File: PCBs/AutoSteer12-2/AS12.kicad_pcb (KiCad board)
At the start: 2 copper layers, 159 x 152 mm, 88 parts, among them IC1 PCA9306DCUR, IC2 XL2596, IC3 AZ1117, J1 ADS1115, J10 Conn_01x08_Female, J11 Teensy_Ethernet, J12 HR911105A, J13 Conn_01x15_Female, J14 Conn_01x08_Female, J15 Motor 2, J16 Motor 1, J17 SF_F9P_left, J18 ArduSimple_tl, J19 ArduSimple_bl, J2 WemosD1_left, J20 SF_F9P_right, J21 ArduSimple_tr, J22 ArduSimple_br, J23 Grove, J24 WemosD1_right, J25 RS485, J3 DT13-12PA, J4 CMPS14, J5 BNO080_left, J6 BNO080_right, J7 I2C-3V3, J8 I2C-3V3, J9 Conn_01x15_Female, K1 HF3FF_012-1ZST, M1 CMPS14_no_pins, Q1 BC847, U1 PC817X2CSP9F, U2 PC817X2CSP9F, U3 PC817X2CSP9F, U4 CC6900SO-10A, U6 MAX3485EESA+T, U7 PC817X2CSP9F

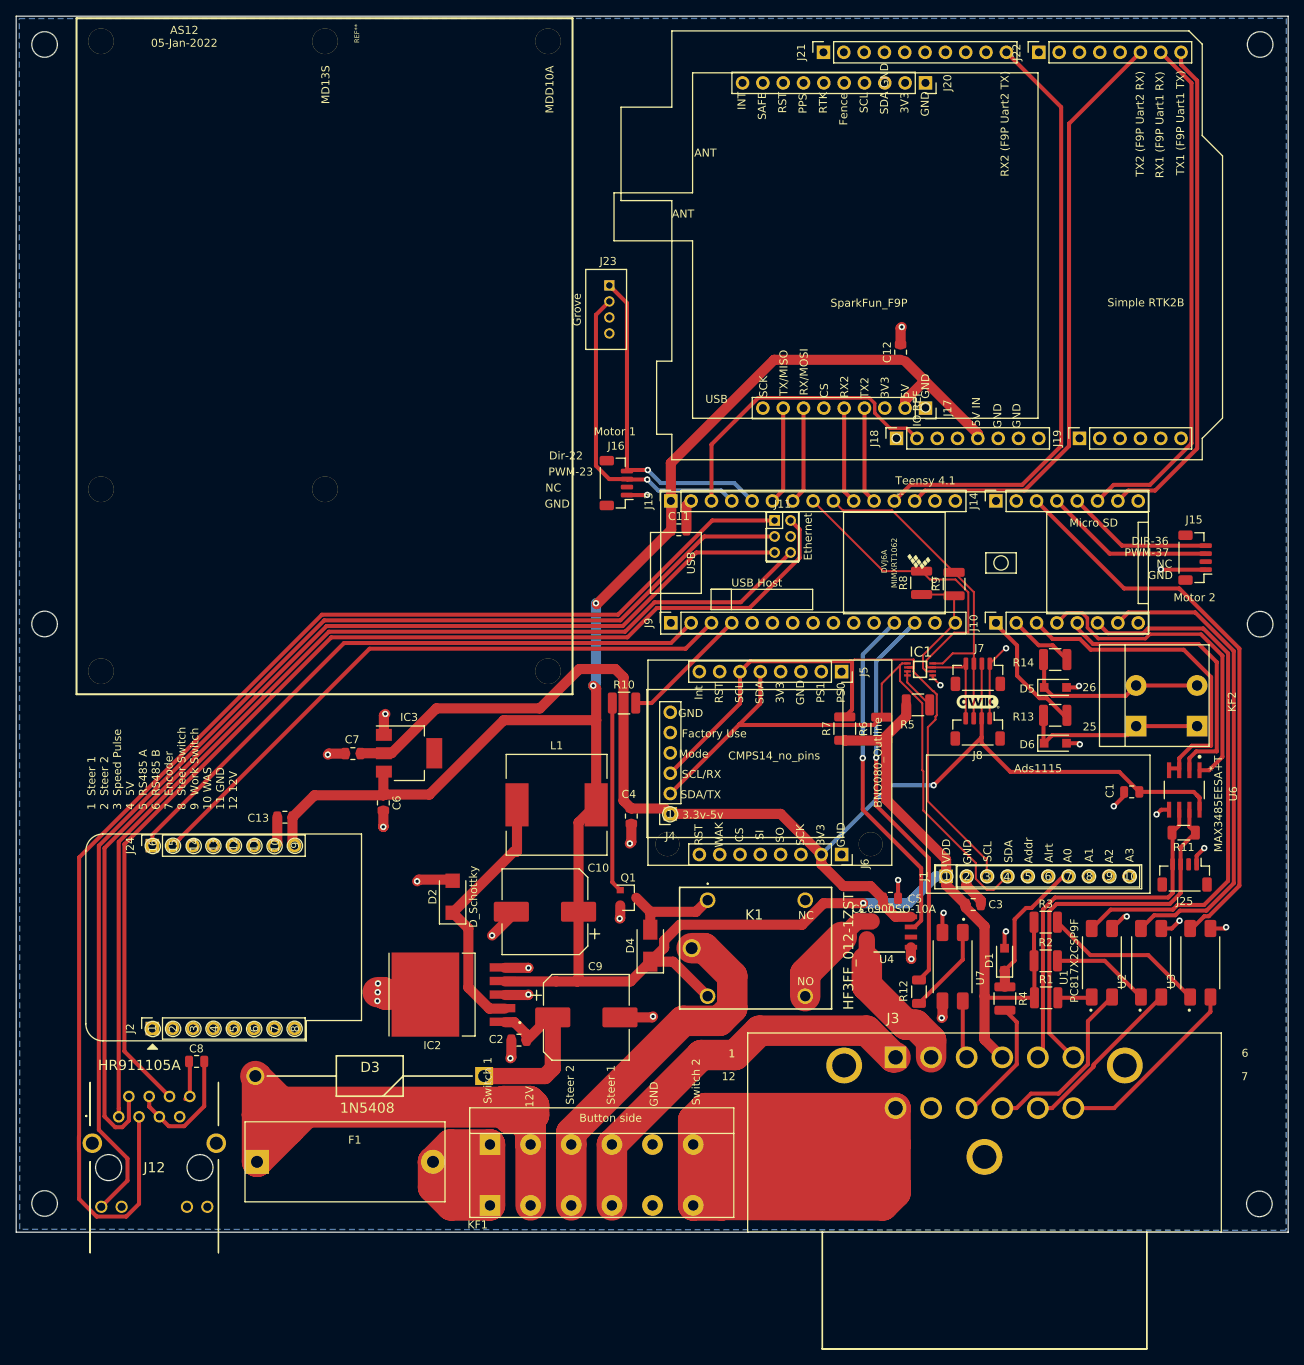
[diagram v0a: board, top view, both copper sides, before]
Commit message: fixed I2C connection
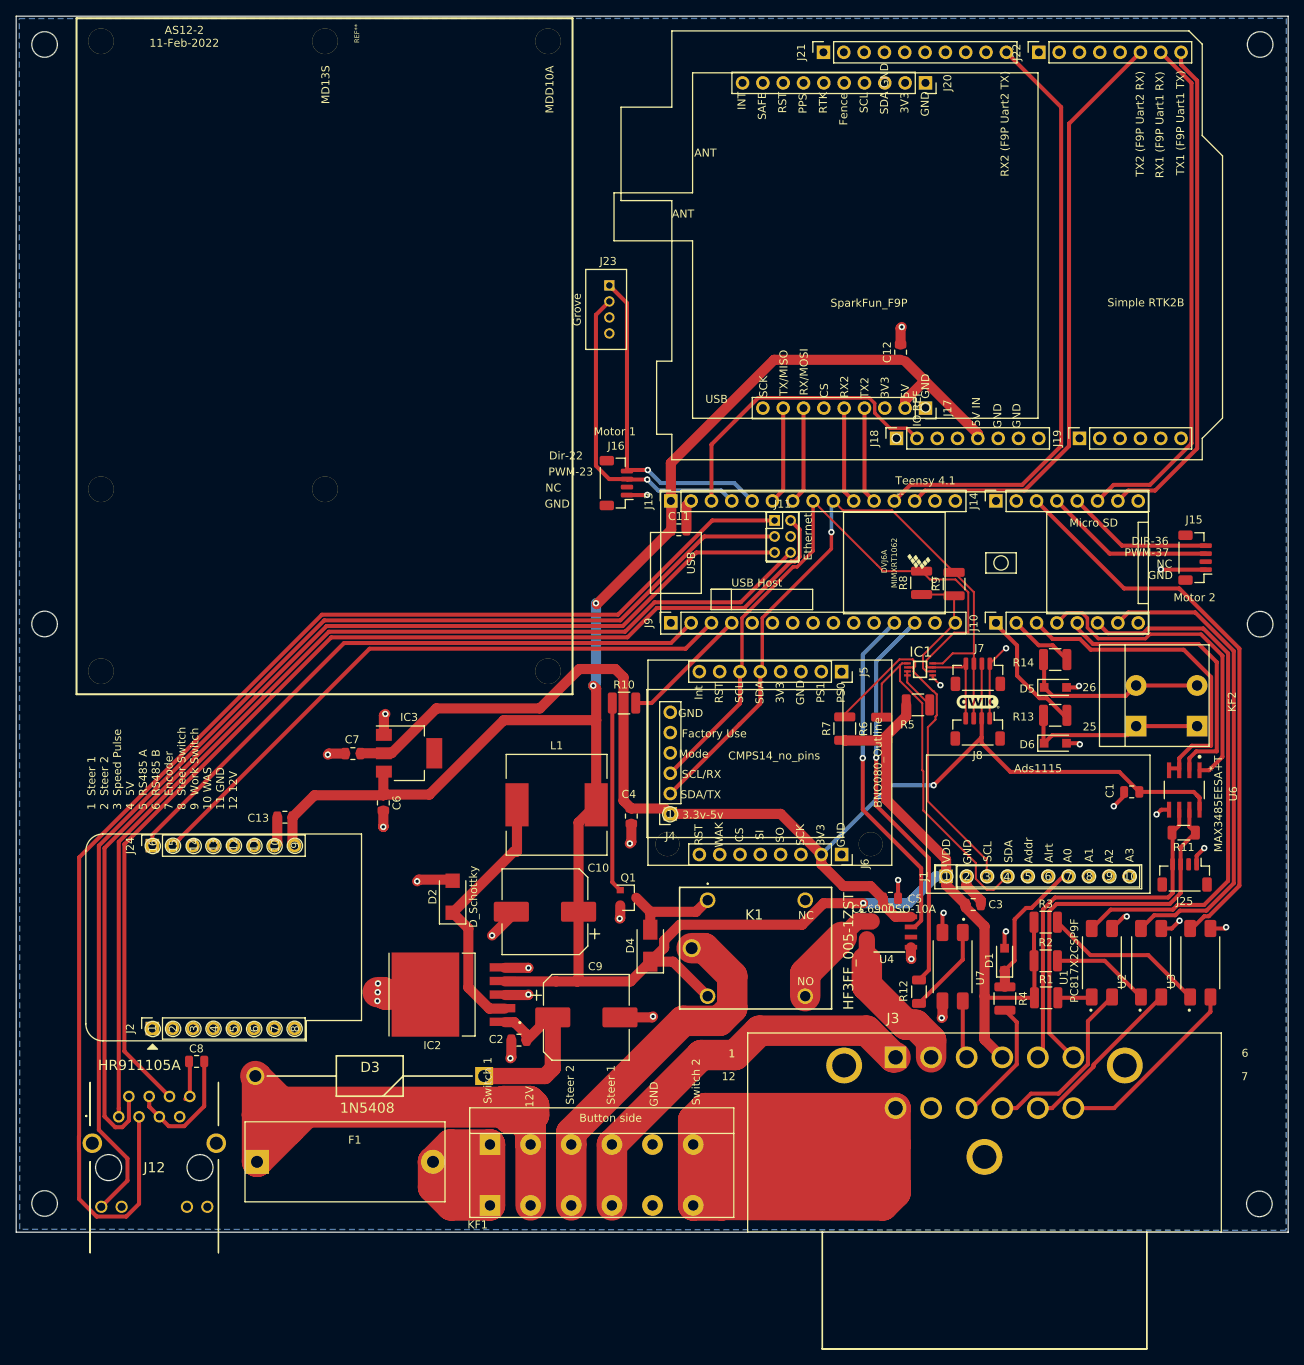
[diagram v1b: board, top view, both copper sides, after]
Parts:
- K1: value HF3FF_012-1ZST -> HF3FF_005-1ZST
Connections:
- J4 pad 2: Net-(IC1-Pad5) -> Net-(IC1-Pad4)
- J4 pad 3: Net-(IC1-Pad6) -> Net-(IC1-Pad3)
- J5 pad 5: Net-(IC1-Pad5) -> Net-(IC1-Pad4)
- J5 pad 6: Net-(IC1-Pad6) -> Net-(IC1-Pad3)
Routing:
- net Net-(IC1-Pad4): track 43.7 -> 88.8 mm, vias 0 -> 1
- net Net-(IC1-Pad3): track 48.6 -> 90.3 mm
- net Net-(IC1-Pad5): track 82.3 -> 44.2 mm
- net Net-(IC1-Pad6): track 79.4 -> 44.7 mm
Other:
- board text added: "AS12-2 11-Feb-2022"
- board text removed: "AS12 05-Jan-2022"
